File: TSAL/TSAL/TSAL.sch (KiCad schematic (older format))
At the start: 15 parts, among them J1 Conn_01x02, J2 Conn_01x02, J3 Conn_01x02, J4 Conn_01x02, Q1 Q_NMOS_GDS, U1 LTV-817S, U2 LM555xM

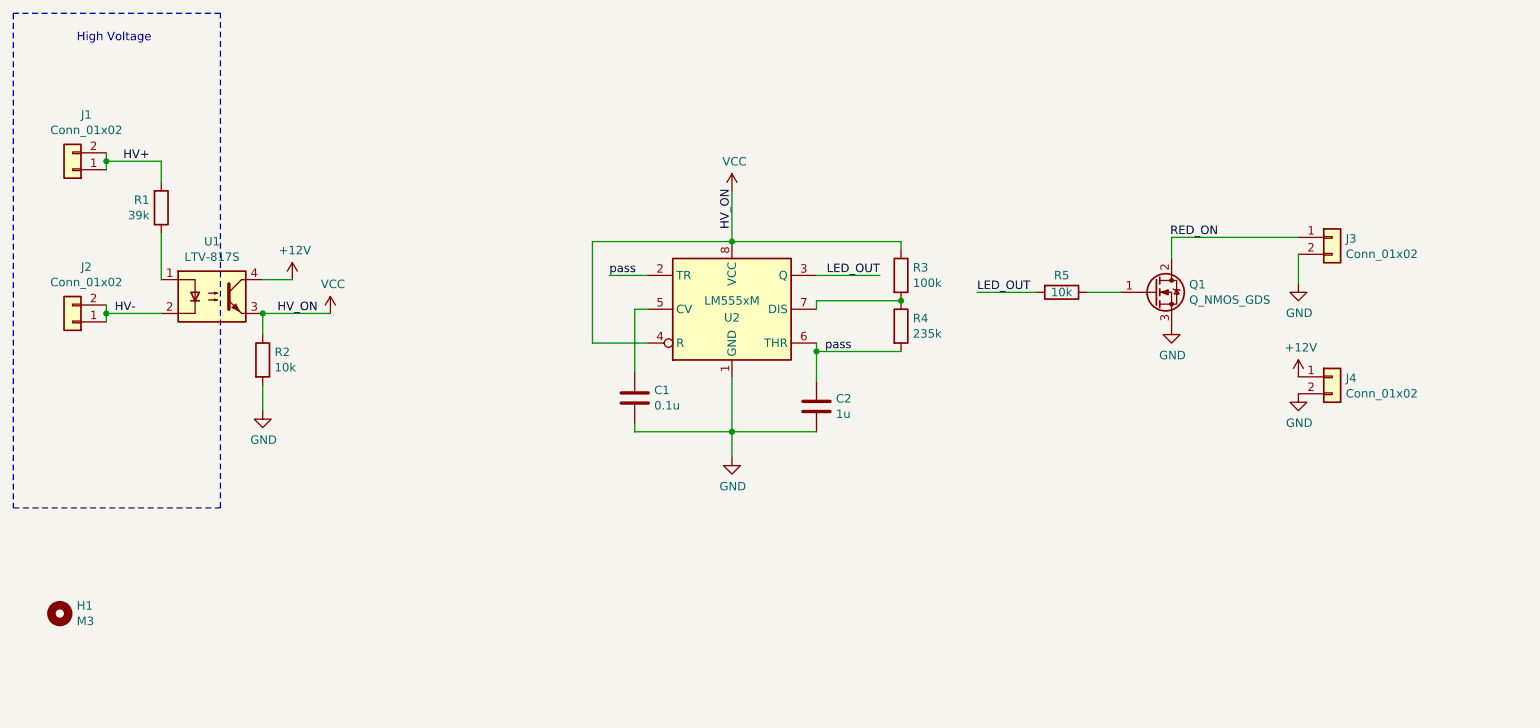
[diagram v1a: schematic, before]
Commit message: change to CC driver
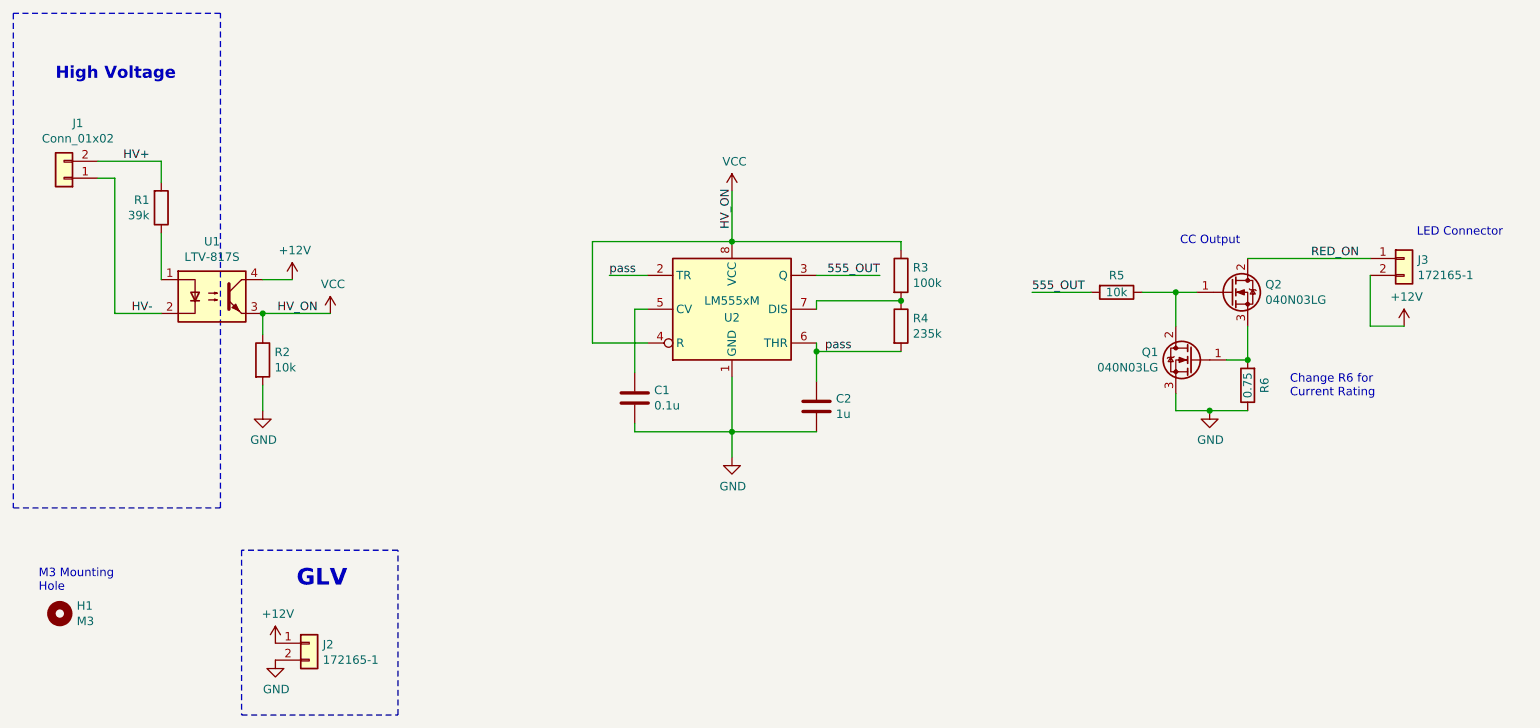
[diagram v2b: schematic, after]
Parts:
- removed J4: Conn_01x02, Connector_TE-Connectivity:TE_MATE-N-LOK_1-770866-x_1x02_P4.14mm_Vertical, symbol Connector_Generic:Conn_01x02
- added Q2: 040N03LG, Package_TO_SOT_SMD:TO-252-3_TabPin2, symbol Device:Q_NMOS_GDS
- added R6: 0.75, Resistor_SMD:R_2512_6332Metric_Pad1.52x3.35mm_HandSolder, symbol Device:R
- J1: footprint Connector_TE-Connectivity:TE_MATE-N-LOK_1-770866-x_1x02_P4.14mm_Vertical -> Connector_Hirose:Hirose_DF63R-2P-3.96DSA_1x02_P3.96mm_Vertical
- J2, J3: value Conn_01x02 -> 172165-1
- Q1: value Q_NMOS_GDS -> 040N03LG
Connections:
- net +12V: now also J2.1 (Pin_1), J3.2 (Pin_2)
- net GND: now also J2.2 (Pin_2), R6.1; no longer J3.2 (Pin_2)
- net HV+: no longer J1.1 (Pin_1)
- net HV-: now also J1.1 (Pin_1); no longer J2.1 (Pin_1), J2.2 (Pin_2)
- net RED_ON: now also Q2.2 (D); no longer Q1.2 (D)
- net at Q1.1 (G): now also Q2.3 (S), R6.2; no longer R5.1
- net LED_OUT renamed 555_OUT
- new net: Q1.2 (D), Q2.1 (G), R5.1
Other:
- note added: "CC Output"
- note added: "Change R6 for \nCurrent Rating"
- note added: "GLV"
- note added: "LED Connector\n"
- note added: "M3 Mounting\nHole"
- moved on the sheet: J1, J3, Q1, R5
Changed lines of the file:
@@
 L Device:R R5
 U 1 1 5F98E1B6
-P 7175 3050
-F 0 "R5" V 7075 3050 50  0000 C CNN
-F 1 "10k" V 7175 3050 50  0000 C CNN
-F 2 "Resistor_SMD:R_0603_1608Metric_Pad1.05x0.95mm_HandSolder" V 7105 3050 50  0001 C CNN
-F 3 "~" H 7175 3050 50  0001 C CNN
-	1    7175 3050
+P 7500 3050
+F 0 "R5" V 7400 3050 50  0000 C CNN
+F 1 "10k" V 7500 3050 50  0000 C CNN
+F 2 "Resistor_SMD:R_0603_1608Metric_Pad1.05x0.95mm_HandSolder" V 7430 3050 50  0001 C CNN
+F 3 "~" H 7500 3050 50  0001 C CNN
+	1    7500 3050
 	0    1    1    0
 $EndComp
@@
 L Device:Q_NMOS_GDS Q1
 U 1 1 5F98B2DE
-P 7725 3050
-F 0 "Q1" H 7929 3096 50  0000 L CNN
-F 1 "Q_NMOS_GDS" H 7929 3005 50  0000 L CNN
-F 2 "Package_TO_SOT_SMD:TO-252-3_TabPin2" H 7925 3150 50  0001 C CNN
-F 3 "~" H 7725 3050 50  0001 C CNN
-	1    7725 3050
-	1    0    0    -1
+P 7950 3450
+F 0 "Q1" H 8154 3496 50  0000 L CNN
+F 1 "040N03LG" H 8154 3405 50  0000 L CNN
+F 2 "Package_TO_SOT_SMD:TO-252-3_TabPin2" H 8150 3550 50  0001 C CNN
+F 3 "https://media.digikey.com/pdf/Data%20Sheets/Infineon%20PDFs/IPD040N03LG_rev1.01.pdf" H 7950 3450 50  0001 C CNN
+	1    7950 3450
+	-1   0    0    -1
 $EndComp
 $Comp
 L power:GND #PWR0102
 U 1 1 5F98F10A
-P 7825 3250
-F 0 "#PWR0102" H 7825 3000 50  0001 C CNN
-F 1 "GND" H 7830 3077 50  0000 C CNN
-F 2 "" H 7825 3250 50  0001 C CNN
-F 3 "" H 7825 3250 50  0001 C CNN
-	1    7825 3250
-	1    0    0    -1
-$EndComp
-Wire Wire Line
-	7525 3050 7325 3050
-Text Label 8100 2725 2    50   ~ 0
+P 8050 3750
+F 0 "#PWR0102" H 8050 3500 50  0001 C CNN
+F 1 "GND" H 8055 3577 50  0000 C CNN
+F 2 "" H 8050 3750 50  0001 C CNN
+F 3 "" H 8050 3750 50  0001 C CNN
+	1    8050 3750
+	1    0    0    -1
+$EndComp
+Text Label 8650 2850 0    50   ~ 0
 RED_ON
-Wire Wire Line
-	7825 2725 7825 2850
 $Comp
 L Connector_Generic:Conn_01x02 J3
 U 1 1 5F996B98
-P 8775 2725
-F 0 "J3" H 8855 2717 50  0000 L CNN
-F 1 "Conn_01x02" H 8855 2626 50  0000 L CNN
-F 2 "Connector_TE-Connectivity:TE_MATE-N-LOK_1-770866-x_1x02_P4.14mm_Vertical" H 8775 2725 50  0001 C CNN
-F 3 "~" H 8775 2725 50  0001 C CNN
-	1    8775 2725
-	1    0    0    -1
-$EndComp
-$Comp
-L power:GND #PWR0103
-U 1 1 5F99726C
-P 8575 3000
-F 0 "#PWR0103" H 8575 2750 50  0001 C CNN
-F 1 "GND" H 8580 2827 50  0000 C CNN
-F 2 "" H 8575 3000 50  0001 C CNN
-F 3 "" H 8575 3000 50  0001 C CNN
-	1    8575 3000
-	1    0    0    -1
-$EndComp
-Wire Wire Line
-	8575 3000 8575 2825
+P 9200 2850
+F 0 "J3" H 9280 2842 50  0000 L CNN
+F 1 "172165-1" H 9280 2751 50  0000 L CNN
+F 2 "Connector_TE-Connectivity:TE_MATE-N-LOK_1-770866-x_1x02_P4.14mm_Vertical" H 9200 2850 50  0001 C CNN
+F 3 "~" H 9200 2850 50  0001 C CNN
+	1    9200 2850
+	1    0    0    -1
+$EndComp
 Wire Wire Line
 	4725 3350 4400 3350
@@
 	5725 3400 6225 3400
 Text Label 6100 2950 2    50   ~ 0
-LED_OUT
+555_OUT
 Wire Wire Line
 	6100 2950 5725 2950
-Text Label 6675 3050 0    50   ~ 0
-LED_OUT
-Wire Wire Line
-	6675 3050 7025 3050
-Wire Wire Line
-	8575 2725 7825 2725
+Text Label 7000 3050 0    50   ~ 0
+555_OUT
+Wire Wire Line
+	7000 3050 7350 3050
 $Comp
 L power:VCC #PWR0104
@@
 L Connector_Generic:Conn_01x02 J1
 U 1 1 5F9BB97B
-P 1325 2325
-F 0 "J1" H 1243 2000 50  0000 C CNN
-F 1 "Conn_01x02" H 1243 2091 50  0000 C CNN
-F 2 "Connector_TE-Connectivity:TE_MATE-N-LOK_1-770866-x_1x02_P4.14mm_Vertical" H 1325 2325 50  0001 C CNN
-F 3 "~" H 1325 2325 50  0001 C CNN
-	1    1325 2325
+P 1275 2375
+F 0 "J1" H 1193 2050 50  0000 C CNN
+F 1 "Conn_01x02" H 1193 2141 50  0000 C CNN
+F 2 "Connector_Hirose:Hirose_DF63R-2P-3.96DSA_1x02_P3.96mm_Vertical" H 1275 2375 50  0001 C CNN
+F 3 "~" H 1275 2375 50  0001 C CNN
+	1    1275 2375
 	-1   0    0    1
 $EndComp
-Wire Wire Line
-	1525 2225 1525 2275
-Wire Wire Line
-	1525 2275 1850 2275
-Wire Wire Line
-	1850 2275 1850 2400
-Connection ~ 1525 2275
-Wire Wire Line
-	1525 2275 1525 2325
-$Comp
-L Connector_Generic:Conn_01x02 J2
-U 1 1 5F9BEA2F
-P 1325 3225
-F 0 "J2" H 1243 2900 50  0000 C CNN
-F 1 "Conn_01x02" H 1243 2991 50  0000 C CNN
-F 2 "Connector_TE-Connectivity:TE_MATE-N-LOK_1-770866-x_1x02_P4.14mm_Vertical" H 1325 3225 50  0001 C CNN
-F 3 "~" H 1325 3225 50  0001 C CNN
-	1    1325 3225
-	-1   0    0    1
-$EndComp
-Wire Wire Line
-	1525 3125 1525 3175
-Wire Wire Line
-	1850 3175 1525 3175
-Connection ~ 1525 3175
-Wire Wire Line
-	1525 3175 1525 3225
-Text Label 1575 3175 0    50   ~ 0
+Text Label 1675 3175 0    50   ~ 0
 HV-
 Text Label 1625 2275 0    50   ~ 0
@@
 Wire Notes Line width 20
 	975  4325 2200 4325
-Text Notes 1350 1575 0    50   ~ 0
+Text Notes 1225 1800 0    71   ~ 14
 High Voltage
 Wire Wire Line
 	4500 2950 4725 2950
-$Comp
-L Connector_Generic:Conn_01x02 J4
-U 1 1 5F9D59EC
-P 8775 3550
-F 0 "J4" H 8855 3542 50  0000 L CNN
-F 1 "Conn_01x02" H 8855 3451 50  0000 L CNN
-F 2 "Connector_TE-Connectivity:TE_MATE-N-LOK_1-770866-x_1x02_P4.14mm_Vertical" H 8775 3550 50  0001 C CNN
-F 3 "~" H 8775 3550 50  0001 C CNN
-	1    8775 3550
-	1    0    0    -1
-$EndComp
 $Comp
 L power:+12V #PWR0108
 U 1 1 5F9D6F6B
-P 8575 3550
-F 0 "#PWR0108" H 8575 3400 50  0001 C CNN
-F 1 "+12V" H 8590 3723 50  0000 C CNN
-F 2 "" H 8575 3550 50  0001 C CNN
-F 3 "" H 8575 3550 50  0001 C CNN
-	1    8575 3550
+P 2525 5125
+F 0 "#PWR0108" H 2525 4975 50  0001 C CNN
+F 1 "+12V" H 2540 5298 50  0000 C CNN
+F 2 "" H 2525 5125 50  0001 C CNN
+F 3 "" H 2525 5125 50  0001 C CNN
+	1    2525 5125
 	1    0    0    -1
 $EndComp
@@
 L power:GND #PWR0109
 U 1 1 5F9D73CE
-P 8575 3650
-F 0 "#PWR0109" H 8575 3400 50  0001 C CNN
-F 1 "GND" H 8580 3477 50  0000 C CNN
-F 2 "" H 8575 3650 50  0001 C CNN
-F 3 "" H 8575 3650 50  0001 C CNN
-	1    8575 3650
+P 2525 5225
+F 0 "#PWR0109" H 2525 4975 50  0001 C CNN
+F 1 "GND" H 2530 5052 50  0000 C CNN
+F 2 "" H 2525 5225 50  0001 C CNN
+F 3 "" H 2525 5225 50  0001 C CNN
+	1    2525 5225
 	1    0    0    -1
 $EndComp
@@
 	1    0    0    -1
 $EndComp
+$Comp
+L Device:R R6
+U 1 1 5FA1ACEA
+P 8275 3600
+F 0 "R6" V 8175 3600 50  0000 C CNN
+F 1 "0.75" V 8275 3600 50  0000 C CNN
+F 2 "Resistor_SMD:R_2512_6332Metric_Pad1.52x3.35mm_HandSolder" V 8205 3600 50  0001 C CNN
+F 3 "~" H 8275 3600 50  0001 C CNN
+	1    8275 3600
+	-1   0    0    1
+$EndComp
+Wire Wire Line
+	1850 2275 1850 2400
+Wire Wire Line
+	1850 3175 1575 3175
+Wire Wire Line
+	1475 2275 1850 2275
+Wire Wire Line
+	1575 3175 1575 2375
+Wire Wire Line
+	1575 2375 1475 2375
+$Comp
+L power:+12V #PWR0103
+U 1 1 5FA35B57
+P 9200 3250
+F 0 "#PWR0103" H 9200 3100 50  0001 C CNN
+F 1 "+12V" H 9215 3423 50  0000 C CNN
+F 2 "" H 9200 3250 50  0001 C CNN
+F 3 "" H 9200 3250 50  0001 C CNN
+	1    9200 3250
+	1    0    0    -1
+$EndComp
+Wire Wire Line
+	9200 3250 9000 3250
+Wire Wire Line
+	9000 2950 9000 3250
+$Comp
+L Device:Q_NMOS_GDS Q2
+U 1 1 5FA4B7C9
+P 8175 3050
+F 0 "Q2" H 8379 3096 50  0000 L CNN
+F 1 "040N03LG" H 8379 3005 50  0000 L CNN
+F 2 "Package_TO_SOT_SMD:TO-252-3_TabPin2" H 8375 3150 50  0001 C CNN
+F 3 "https://media.digikey.com/pdf/Data%20Sheets/Infineon%20PDFs/IPD040N03LG_rev1.01.pdf" H 8175 3050 50  0001 C CNN
+	1    8175 3050
+	1    0    0    -1
+$EndComp
+Wire Wire Line
+	8150 3450 8275 3450
+Wire Wire Line
+	8275 3450 8275 3250
+Connection ~ 8275 3450
+Wire Wire Line
+	8275 3750 8050 3750
+Wire Wire Line
+	7850 3750 7850 3650
+Connection ~ 8050 3750
+Wire Wire Line
+	8050 3750 7850 3750
+Wire Wire Line
+	8275 2850 9000 2850
+Wire Wire Line
+	7650 3050 7850 3050
+Wire Wire Line
+	7850 3250 7850 3050
+Connection ~ 7850 3050
+Wire Wire Line
+	7850 3050 7975 3050
+$Comp
+L Connector_Generic:Conn_01x02 J2
+U 1 1 5FA7ECF0
+P 2725 5125
+F 0 "J2" H 2805 5117 50  0000 L CNN
+F 1 "172165-1" H 2805 5026 50  0000 L CNN
+F 2 "Connector_TE-Connectivity:TE_MATE-N-LOK_1-770866-x_1x02_P4.14mm_Vertical" H 2725 5125 50  0001 C CNN
+F 3 "~" H 2725 5125 50  0001 C CNN
+	1    2725 5125
+	1    0    0    -1
+$EndComp
+Text Notes 2650 4800 0    98   ~ 20
+GLV
+Wire Notes Line width 24
+	2325 4575 2325 5550
+Wire Notes Line width 24
+	2325 5550 3250 5550
+Wire Notes Line width 24
+	3250 5550 3250 4575
+Wire Notes Line width 24
+	3250 4575 2325 4575
+Text Notes 1125 4825 0    50   ~ 0
+M3 Mounting\nHole
+Text Notes 7875 2775 0    50   ~ 0
+CC Output
+Text Notes 8525 3675 0    50   ~ 0
+Change R6 for \nCurrent Rating
+Text Notes 9275 2725 0    50   ~ 0
+LED Connector\n
 $EndSCHEMATC

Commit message: initial commit
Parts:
- added C3: 0.1u, Capacitor_SMD:C_0603_1608Metric_Pad1.05x0.95mm_HandSolder, symbol Device:C
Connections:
- net GND: now also C3.2
- net VCC: now also C3.1
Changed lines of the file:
@@
 Text Label 5225 2675 1    50   ~ 0
 HV_ON
-Wire Wire Line
-	5225 2450 5225 2750
 $Comp
 L Device:R R5
@@
 L power:VCC #PWR0104
 U 1 1 5F9896F1
-P 5225 2450
-F 0 "#PWR0104" H 5225 2300 50  0001 C CNN
-F 1 "VCC" H 5240 2623 50  0000 C CNN
-F 2 "" H 5225 2450 50  0001 C CNN
-F 3 "" H 5225 2450 50  0001 C CNN
-	1    5225 2450
+P 5225 2225
+F 0 "#PWR0104" H 5225 2075 50  0001 C CNN
+F 1 "VCC" H 5240 2398 50  0000 C CNN
+F 2 "" H 5225 2225 50  0001 C CNN
+F 3 "" H 5225 2225 50  0001 C CNN
+	1    5225 2225
 	1    0    0    -1
 $EndComp
@@
 Text Notes 9275 2725 0    50   ~ 0
 LED Connector\n
+$Comp
+L Device:C C3
+U 1 1 5FACE85F
+P 4700 2375
+F 0 "C3" H 4815 2421 50  0000 L CNN
+F 1 "0.1u" H 4815 2330 50  0000 L CNN
+F 2 "Capacitor_SMD:C_0603_1608Metric_Pad1.05x0.95mm_HandSolder" H 4738 2225 50  0001 C CNN
+F 3 "~" H 4700 2375 50  0001 C CNN
+	1    4700 2375
+	1    0    0    -1
+$EndComp
+Wire Wire Line
+	5225 2225 4700 2225
+Wire Wire Line
+	5225 2225 5225 2750
+Connection ~ 5225 2225
+$Comp
+L power:GND #PWR0110
+U 1 1 5FAD4BE3
+P 4700 2525
+F 0 "#PWR0110" H 4700 2275 50  0001 C CNN
+F 1 "GND" H 4705 2352 50  0000 C CNN
+F 2 "" H 4700 2525 50  0001 C CNN
+F 3 "" H 4700 2525 50  0001 C CNN
+	1    4700 2525
+	1    0    0    -1
+$EndComp
 $EndSCHEMATC
